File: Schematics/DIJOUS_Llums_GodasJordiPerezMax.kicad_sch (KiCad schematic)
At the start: 101 parts, among them J1 Conn_01x05_Socket, J2 Conn_01x03, J3 Conn_01x06, J4 Screw_Terminal_01x02, J5 Conn_01x05, J6 DE9_Plug, J7 Conn_01x02, J8 Conn_01x06_Socket, K1 G5LE-1 DC12, K2 G5LE-1 DC12, Q1 ZXTN19020DFFTA, Q2 ZXTN19020DFFTA, Q3 ZXTN19020DFFTA, Q4 Si7336ADP, Q5 Si7336ADP, Q6 ZXTN19020DFFTA, Q7 ZXTN19020DFFTA, Q8 Si7336ADP, Q9 Si7336ADP, U1 PCA9306D, U2 PIC18F2580-I/SO, U3 LM2596T-ADJ, U4 ADP7112ACBZ-3.3-R7, U5 MCP2551-I-SN, U6 ADM7172ACPZ-5.0-R7, U7 LT6202CS5

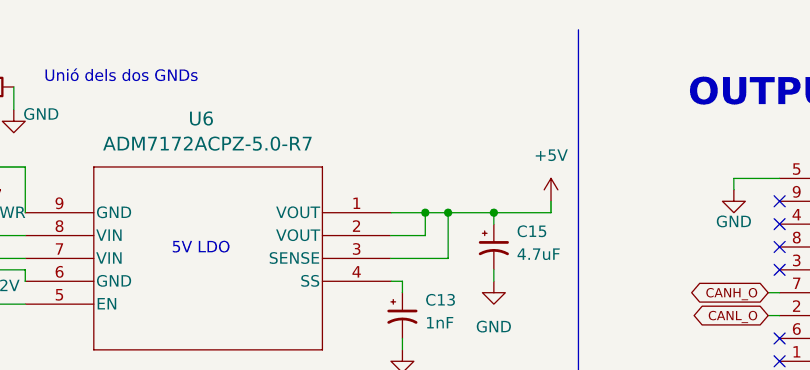
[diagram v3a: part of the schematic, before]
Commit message: Update esquemático
Versión 2.0 del esquemático. Cambios notables respecto a la semana pasada
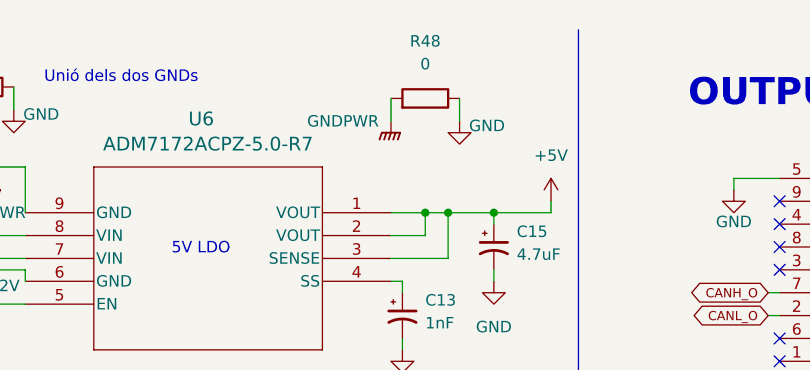
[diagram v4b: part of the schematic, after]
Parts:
- added R48: 0, Resistor_SMD:R_0603_1608Metric, symbol Device:R
- R23: footprint (none) -> Resistor_SMD:R_0603_1608Metric
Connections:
- net GND: now also R48.1
- net GNDPWR: now also R48.2
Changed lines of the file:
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@@
 	(wire
 		(pts
+			(xy 266.7 22.86) (xy 266.7 20.32)
+		)
+		(stroke
+			(width 0)
+			(type default)
+		)
+	)
+	(wire
+		(pts
 			(xy 339.09 179.07) (xy 339.09 184.15)
 		)
@@
 	(wire
 		(pts
+			(xy 274.32 22.86) (xy 274.32 20.32)
+		)
+		(stroke
+			(width 0)
+			(type default)
+		)
+	)
+	(wire
+		(pts
 			(xy 243.84 257.81) (xy 243.84 260.35)
 		)
@@
 			)
 		)
-		(property "Footprint" ""
+		(property "Footprint" "Resistor_SMD:R_0603_1608Metric"
 			(at 220.98 20.828 90)
 			(effects
@@
 	)
 	(symbol
+		(lib_id "power:GNDPWR")
+		(at 266.7 22.86 0)
+		(unit 1)
+		(exclude_from_sim no)
+		(in_bom yes)
+		(on_board yes)
+		(dnp no)
+		(property "Reference" "#PWR029"
+			(at 266.7 27.94 0)
+			(effects
+				(font
+					(size 1.27 1.27)
+				)
+				(hide yes)
+			)
+		)
+		(property "Value" "GNDPWR"
+			(at 261.366 22.86 0)
+			(effects
+				(font
+					(size 1.27 1.27)
+				)
+			)
+		)
+		(property "Footprint" ""
+			(at 266.7 24.13 0)
+			(effects
+				(font
+					(size 1.27 1.27)
+				)
+				(hide yes)
+			)
+		)
+		(property "Datasheet" ""
+			(at 266.7 24.13 0)
+			(effects
+				(font
+					(size 1.27 1.27)
+				)
+				(hide yes)
+			)
+		)
+		(property "Description" "Power symbol creates a global label with name \"GNDPWR\" , global ground"
+			(at 266.7 22.86 0)
+			(effects
+				(font
+					(size 1.27 1.27)
+				)
+				(hide yes)
+			)
+		)
+		(pin "1"
+		)
+		(instances
+			(project "DIJOUS_Llums_GodasJordiPerezMax"
+				(path "/572cad61-fefa-4039-8286-3cbe6ea7f51a"
+					(reference "#PWR029")
+					(unit 1)
+				)
+			)
+		)
+	)
+	(symbol
 		(lib_id "power:+3.3V")
 		(at 52.07 143.51 0)
@@
 	(symbol
 		(lib_id "power:GND")
+		(at 274.32 22.86 0)
+		(mirror y)
+		(unit 1)
+		(exclude_from_sim no)
+		(in_bom yes)
+		(on_board yes)
+		(dnp no)
+		(property "Reference" "#PWR0102"
+			(at 274.32 29.21 0)
+			(effects
+				(font
+					(size 1.27 1.27)
+				)
+				(hide yes)
+			)
+		)
+		(property "Value" "GND"
+			(at 277.368 23.368 0)
+			(effects
+				(font
+					(size 1.27 1.27)
+				)
+			)
+		)
+		(property "Footprint" ""
+			(at 274.32 22.86 0)
+			(effects
+				(font
+					(size 1.27 1.27)
+				)
+				(hide yes)
+			)
+		)
+		(property "Datasheet" ""
+			(at 274.32 22.86 0)
+			(effects
+				(font
+					(size 1.27 1.27)
+				)
+				(hide yes)
+			)
+		)
+		(property "Description" "Power symbol creates a global label with name \"GND\" , ground"
+			(at 274.32 22.86 0)
+			(effects
+				(font
+					(size 1.27 1.27)
+				)
+				(hide yes)
+			)
+		)
+		(pin "1"
+		)
+		(instances
+			(project "DIJOUS_Llums_GodasJordiPerezMax"
+				(path "/572cad61-fefa-4039-8286-3cbe6ea7f51a"
+					(reference "#PWR0102")
+					(unit 1)
+				)
+			)
+		)
+	)
+	(symbol
+		(lib_id "power:GND")
 		(at 58.42 76.2 0)
 		(unit 1)
@@
 					(unit 1)
 				)
+			)
+		)
+	)
+	(symbol
+		(lib_id "Device:R")
+		(at 270.51 20.32 270)
+		(mirror x)
+		(unit 1)
+		(exclude_from_sim no)
+		(in_bom yes)
+		(on_board yes)
+		(dnp no)
+		(property "Reference" "R48"
+			(at 270.51 13.97 90)
+			(effects
+				(font
+					(size 1.27 1.27)
+				)
+			)
+		)
+		(property "Value" "0"
+			(at 270.51 16.51 90)
+			(effects
+				(font
+					(size 1.27 1.27)
+				)
+			)
+		)
+		(property "Footprint" "Resistor_SMD:R_0603_1608Metric"
+			(at 270.51 22.098 90)
+			(effects
+				(font
+					(size 1.27 1.27)
+				)
+				(hide yes)
+			)
+		)
+		(property "Datasheet" "~"
+			(at 270.51 20.32 0)
+			(effects
+				(font
+					(size 1.27 1.27)
+				)
+				(hide yes)
+			)
+		)
+		(property "Description" "Resistor"
+			(at 270.51 20.32 0)
+			(effects
+				(font
+					(size 1.27 1.27)
+				)
+				(hide yes)
+			)
+		)
+		(pin "1"
+		)
+		(pin "2"
+		)
+		(instances
+			(project "DIJOUS_Llums_GodasJordiPerezMax"
+				(path "/572cad61-fefa-4039-8286-3cbe6ea7f51a"
+					(reference "R48")
+					(unit 1)
+				)

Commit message: Update esquemático
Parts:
- removed C10, C9: 2.2uF, Capacitor_SMD:C_1206_3216Metric_Pad1.33x1.80mm_HandSolder, symbol Device:C
- removed R48: 0, Resistor_SMD:R_0603_1608Metric, symbol Device:R
- removed U4: ADP7112ACBZ-3.3-R7, ADP7112ACBZ-3.3-R7:CB-6-15_ADI-M, symbol ADP7112ACBZ-3.3-R7:ADP7112ACBZ-3.3-R7
- added C18: 100uF, Capacitor_SMD:C_1206_3216Metric_Pad1.33x1.80mm_HandSolder, symbol Device:C_Polarized_Small_US
- added D9: 1N4002, Diode_THT:D_DO-41_SOD81_P10.16mm_Horizontal, symbol Diode:1N4002
- added U8: TLV1117-33, Package_TO_SOT_SMD:SOT-223, symbol Regulator_Linear:TLV1117-33
- C11: value 1nF -> 10uF
- R23: footprint Resistor_SMD:R_0603_1608Metric -> (none)
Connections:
- net +3.3V: now also C18.1, D9.2 (A), U8.2 (VO)
- net +5V: now also C11.1, D9.1 (K), U8.3 (VI)
- net GND: now also C18.2, U8.1 (GND)
- net OSC1: no longer names the net of C3.1, U2.9 (OSC1/CLKI/RA7), XTAL1.1
- net OSC2: no longer names the net of C5.1, U2.10 (OSC2/CLKO/RA6), XTAL1.2
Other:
- note removed: "CLOCK"
- moved on the sheet: C14, C3, C5, J1, J4, J5, R1, R13, R16, R17, R2, R3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

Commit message: Update esquemático
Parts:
- J1, J5: footprint Connector_PinHeader_1.00mm:PinHeader_1x05_P1.00mm_Vertical -> Connector_PinHeader_2.54mm:PinHeader_1x05_P2.54mm_Vertical
- J2: footprint Connector_PinHeader_1.00mm:PinHeader_1x03_P1.00mm_Vertical -> Connector_PinHeader_2.54mm:PinHeader_1x03_P2.54mm_Vertical
- J3, J8: footprint Connector_PinHeader_1.00mm:PinHeader_1x06_P1.00mm_Vertical -> Connector_PinHeader_2.54mm:PinHeader_1x06_P2.54mm_Vertical
- J4: footprint Connector_PinHeader_1.00mm:PinHeader_1x02_P1.00mm_Vertical -> TerminalBlock:TerminalBlock_Xinya_XY308-2.54-2P_1x02_P2.54mm_Horizontal
- J7: footprint Connector_PinHeader_1.00mm:PinHeader_1x02_P1.00mm_Vertical -> Connector_PinHeader_2.54mm:PinHeader_1x02_P2.54mm_Vertical
- R23: footprint (none) -> Resistor_SMD:R_0805_2012Metric
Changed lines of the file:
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@@
 			)
 		)
-		(property "Footprint" ""
+		(property "Footprint" "Resistor_SMD:R_0805_2012Metric"
 			(at 220.98 20.828 90)
 			(effects
@@
 			)
 		)
-		(property "Footprint" "Connector_PinHeader_1.00mm:PinHeader_1x06_P1.00mm_Vertical"
+		(property "Footprint" "Connector_PinHeader_2.54mm:PinHeader_1x06_P2.54mm_Vertical"
 			(at 359.41 43.18 0)
 			(effects
@@
 			)
 		)
-		(property "Footprint" "Connector_PinHeader_1.00mm:PinHeader_1x05_P1.00mm_Vertical"
+		(property "Footprint" "Connector_PinHeader_2.54mm:PinHeader_1x05_P2.54mm_Vertical"
 			(at 250.19 190.5 0)
 			(effects
@@
 			)
 		)
-		(property "Footprint" "Connector_PinHeader_1.00mm:PinHeader_1x06_P1.00mm_Vertical"
+		(property "Footprint" "Connector_PinHeader_2.54mm:PinHeader_1x06_P2.54mm_Vertical"
 			(at 27.94 111.76 0)
 			(effects
@@
 			)
 		)
-		(property "Footprint" "Connector_PinHeader_1.00mm:PinHeader_1x05_P1.00mm_Vertical"
+		(property "Footprint" "Connector_PinHeader_2.54mm:PinHeader_1x05_P2.54mm_Vertical"
 			(at 73.66 46.99 0)
 			(effects
@@
 			)
 		)
-		(property "Footprint" "Connector_PinHeader_1.00mm:PinHeader_1x02_P1.00mm_Vertical"
+		(property "Footprint" "TerminalBlock:TerminalBlock_Xinya_XY308-2.54-2P_1x02_P2.54mm_Horizontal"
 			(at 29.21 44.45 0)
 			(effects
@@
 			)
 		)
-		(property "Footprint" "Connector_PinHeader_1.00mm:PinHeader_1x02_P1.00mm_Vertical"
+		(property "Footprint" "Connector_PinHeader_2.54mm:PinHeader_1x02_P2.54mm_Vertical"
 			(at 354.33 24.13 0)
 			(effects
@@
 			)
 		)
-		(property "Footprint" "Connector_PinHeader_1.00mm:PinHeader_1x03_P1.00mm_Vertical"
+		(property "Footprint" "Connector_PinHeader_2.54mm:PinHeader_1x03_P2.54mm_Vertical"
 			(at 22.86 204.47 0)
 			(effects

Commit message: Update Schematic
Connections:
- net Shutin: now also R32.1, R33.1; no longer R40.1, U2.2 (RA0/AN0), U7.1 (OUT)
- net BJTbase4: now reaches Q6.1, R14.2
- net BJTemissor4: now reaches K1.2, Q6.2
- net LDO5V_IN: now reaches C8.1, L1.2, R21.2, U6.7 (VIN), U6.8 (VIN)
- net BJTbase5: now reaches Q7.1, R47.2
- net BJTbase2: now reaches Q2.1, R30.2
- net BJTbase1: now reaches Q1.1, R29.2
- net BJTemissor5: now reaches K2.2, Q7.2
- net Buck_IN: now reaches C6.1, D1.1 (K), D2.3 (K), U3.1 (VIN)
- net Buck_OUT: now reaches CR1.1, L1.1, U3.2 (OUT)
- net Buck_FB: now reaches R20.1, R21.1, U3.4 (FB)
- net BJTbase3: now reaches Q3.1, R31.2
- net SHUT_OPV-: now reaches R36.2, R39.2, U7.4 (-IN)
- net SHUT_OPV+: now reaches R33.2, R40.2, U7.3 (+IN)
- net ENABLE: now reaches R11.2, U1.8 (EN)
- net BJTbase11 renamed NMOSbase11
- net BJTbase12 renamed NMOSbase12
- net BJTbase21 renamed NMOSbase21
- net BJTbase22 renamed NMOSbase22
- new net SHUT_OUT: R40.1, U2.2 (RA0/AN0), U7.1 (OUT)
